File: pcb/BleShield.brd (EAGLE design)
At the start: 22.6 x 10 mm, 31 parts, among them U1 ARDUINO_SHIELDNOHOLES, Y1 32.768KHz, 10 PPM

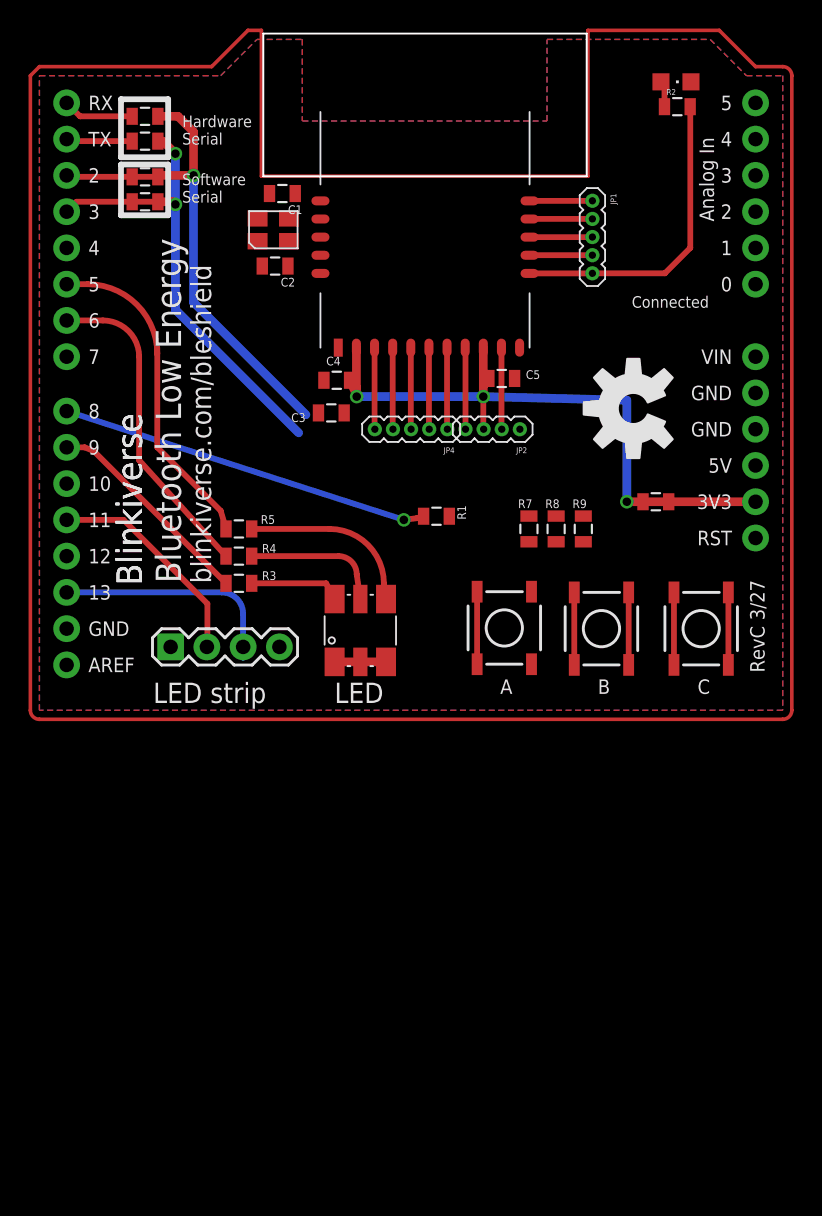
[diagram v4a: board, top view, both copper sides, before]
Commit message: Knocked out everything except crystal pad and RX/TX doublecheck.
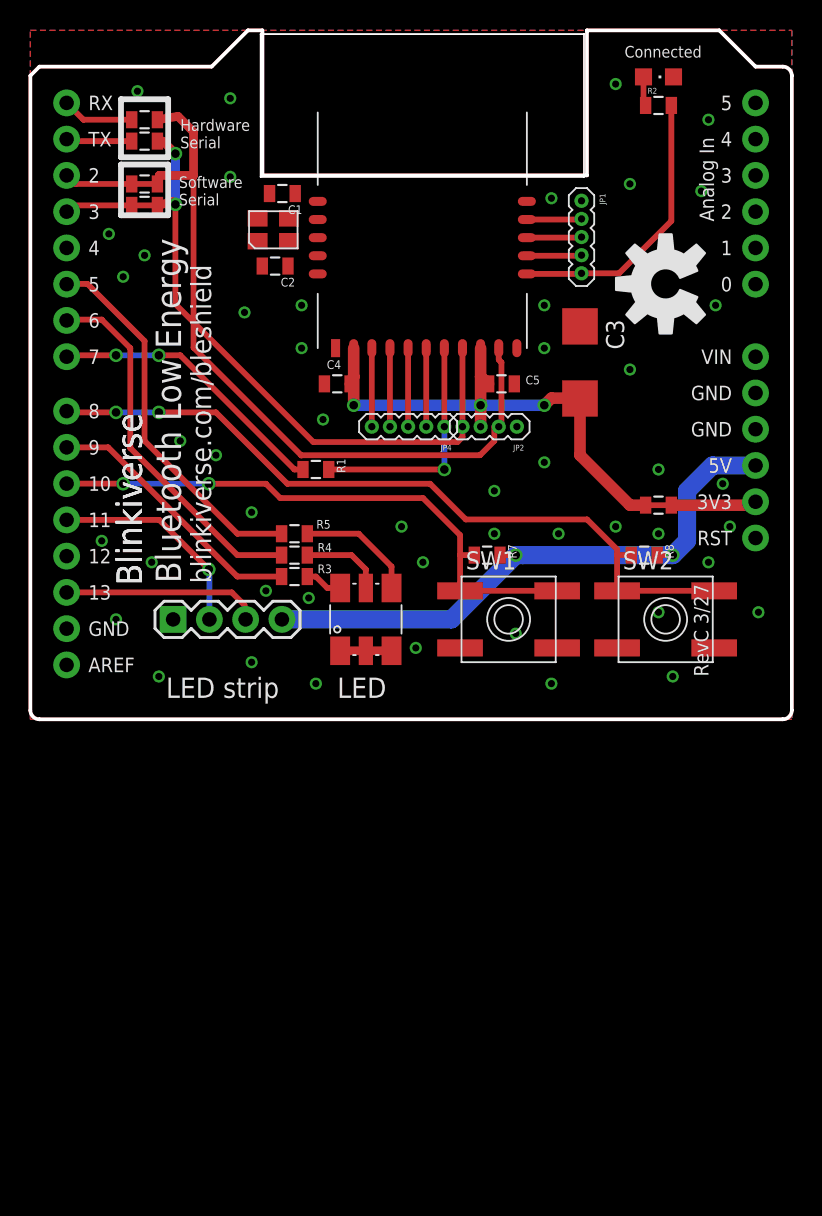
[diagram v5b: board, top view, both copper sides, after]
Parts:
- removed A, B, C: (no value), SparkFun:TACTILE_SWITCH_SMD
- removed R9: 10K, SparkFun:0805
- added SW1, SW2: SPST_TACT-EVQQ2, adafruit:EVQ-Q2
- C3: device SparkFun:0805 -> rcl:C/6032-28R
- moved C3 17.8 mm to (38.5, 25.0), turned to 270 degrees
- moved R1 9.06 mm to (20.0, 17.5)
- moved U$7 9.01 mm to (44.5, 30.5)
- moved R8 6.44 mm to (43.0, 11.5), turned to 0 degrees
- moved R3 3.92 mm to (18.5, 10.0)
- moved R5 3.91 mm to (18.5, 13.0)
- moved R4 3.90 mm to (18.5, 11.5)
- moved R7 3.45 mm to (32.0, 11.5), turned to 0 degrees
- moved LED_STRIP 1.94 mm to (10.0, 7.00)
- moved R2 1.32 mm to (44.0, 43.0)
- moved LED1 1.27 mm to (44.0, 45.0)
- moved RGB_LED 0.87 mm to (23.5, 7.00)
- moved JP1 0.76 mm to (38.6, 36.3)
- moved R12 0.50 mm to (8.00, 37.5)
- moved C5 0.38 mm to (33.0, 23.5)
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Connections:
- removed net SWITCH_C: C.3, C.4, R9.1, U1.D7
- net 3.3V: now also C3.+; no longer C3.2
- net 5V: no longer R9.2
- net GND: now also C3.-, SW1.A, SW1.A', SW2.A, SW2.A'; no longer A.1, A.2, B.1, B.2, C.1, C.2, C3.1
- net RESET: now also U1.D7; no longer U1.D8
- net SWITCH_A: now also SW1.B, SW1.B', U1.D10; no longer A.3, A.4, U1.D12
- net SWITCH_B: now also SW2.B, SW2.B', U1.D8; no longer B.3, B.4, U1.D4
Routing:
- net SWITCH_B: track 5.08 -> 53.3 mm, vias 0 -> 2
- net 5V: track 0.00 -> 41.9 mm, vias 0 -> 2
- net SWITCH_A: track 5.08 -> 40.9 mm, vias 0 -> 2
- net RX: track 40.7 -> 59.3 mm, vias 1 -> 0
- net GND: track 18.3 -> 3.92 mm, vias 0 -> 48
- net TX: track 38.4 -> 50.6 mm
- net N$1: track 5.74 -> 16.6 mm, vias 0 -> 1
- net RESET: track 26.2 -> 19.9 mm, vias 1 -> 2
- net SWITCH_C: track 5.08 -> 0.00 mm
- net N$2: track 6.47 -> 2.63 mm
- net N$6: track 9.64 -> 5.81 mm
- net LED_BLUE: track 15.1 -> 18.8 mm
- net N$5: track 12.0 -> 8.35 mm
- net LED_RED: track 22.4 -> 26.0 mm
- net LED_GREEN: track 23.0 -> 26.4 mm
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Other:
- board size 22.6 x 10 mm -> 53.3 x 48.3 mm

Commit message: Fix RX/TX line assignment
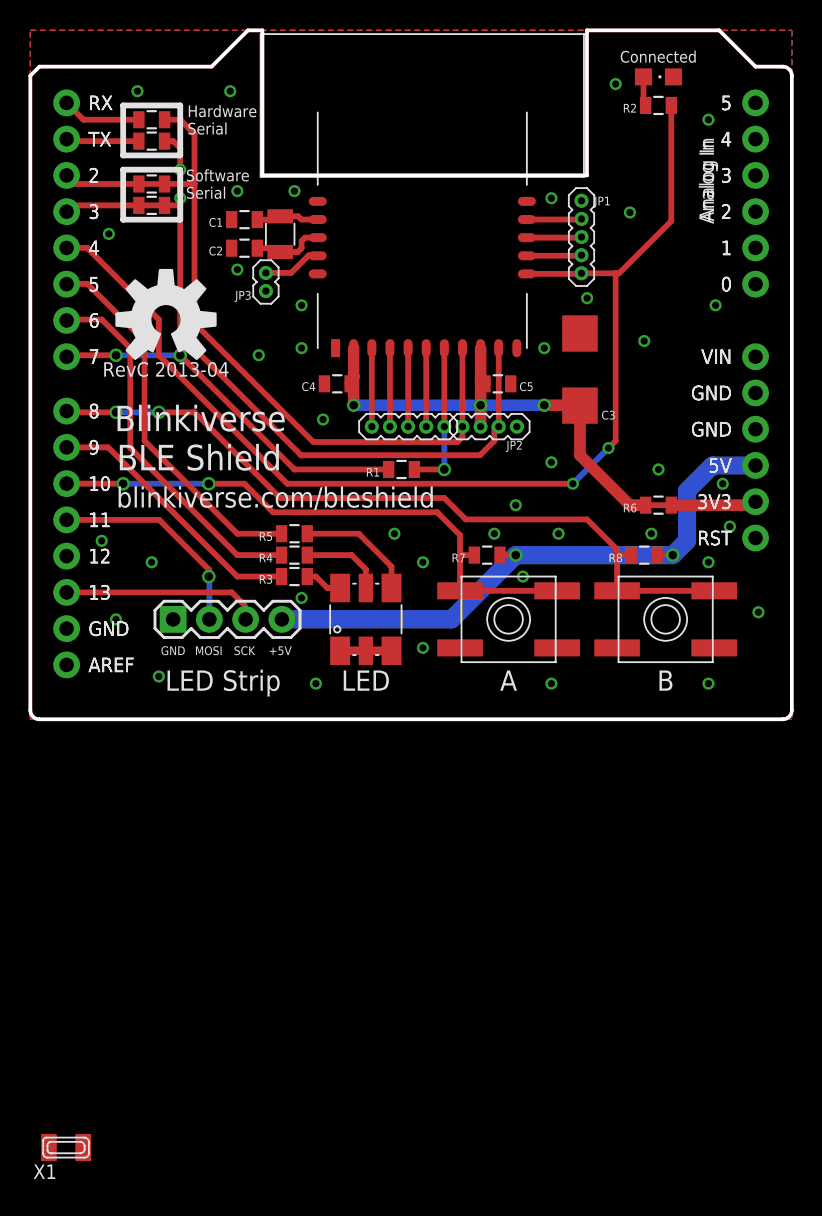
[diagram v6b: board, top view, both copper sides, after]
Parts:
- removed Y1: 32.768KHz, 10 PPM, blinkiverse:XS3225
- added JP3: (no value), BLE:1X02-1.27MM
- added Q1: 32.768K, 10ppm, blinkiverse:CRYSTAL_3215
- added X1: (no value), adafruit:XTAL3215
- moved U$7 35.1 mm to (9.50, 28.0), turned to 0 degrees
- moved R1 6.00 mm to (26.0, 17.5)
- moved C1 3.22 mm to (15.0, 35.0), turned to 0 degrees
- moved C2 2.48 mm to (15.0, 33.0), turned to 0 degrees
- moved C3 0.50 mm to (38.5, 24.5)
- moved R10 0.50 mm to (8.50, 42.0)
- moved R11 0.50 mm to (8.50, 40.5)
- moved R12 0.50 mm to (8.50, 37.5)
- moved R13 0.50 mm to (8.50, 36.0)
- moved C5 0.25 mm to (32.8, 23.5)
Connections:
- removed net N$9: JP1.5, R2.2, U$1.P0_7
- new net CONNECTED: JP1.5, R2.2, U$1.P0_7, U1.D4
- new net N$19: JP3.2, U$1.P2_0
- net GND: now also JP3.1
- net N$3: now also Q1.P$2; no longer Y1.P$3
- net N$4: now also Q1.P$1; no longer Y1.P$1
- net RX: now also JP2.4, U$1.P1_6/TX; no longer JP2.2, U$1.P1_7/RX
- net TX: now also JP2.2, U$1.P1_7/RX; no longer JP2.4, U$1.P1_6/TX
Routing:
- net CONNECTED: track 0.00 -> 79.5 mm, vias 0 -> 2
- net N$9: track 19.8 -> 0.00 mm
- net RESET: track 19.9 -> 25.9 mm
- net N$1: track 16.6 -> 10.6 mm
- net RX: track 59.3 -> 53.6 mm
- net N$4: track 0.00 -> 5.05 mm
- net TX: track 50.6 -> 55.2 mm
- net N$3: track 0.00 -> 4.42 mm
- net N$19: track 0.00 -> 4.15 mm
- net MOSI: track 14.9 -> 15.8 mm
- net 3.3V: track 44.7 -> 43.8 mm
- net N$11: track 4.62 -> 5.12 mm
- net N$10: track 5.05 -> 5.55 mm
- net GND: vias 48 -> 41
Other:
- board text added: "+5V"
- board text added: "0"
- board text added: "1"
- board text added: "10"
- board text added: "11"
- board text added: "12"
- board text added: "13"
- board text added: "2"
- board text added: "3"
- board text added: "3V3"
- board text added: "4"
- board text added: "5"
- board text added: "5V"
- board text added: "6"
- board text added: "7"
- board text added: "8"
- board text added: "9"
- board text added: "A"
- board text added: "AREF"
- board text added: "Analog In"
- board text added: "B"
- board text added: "BLE Shield"
- board text added: "GND"
- board text added: "LED Strip"
- board text added: "MOSI"
- board text added: "RST"
- board text added: "RX"
- board text added: "RevC 2013-04"
- board text added: "SCK"
- board text added: "TX"
- board text added: "VIN"
- board text removed: "Bluetooth Low Energy"
- board text removed: "LED strip"
- board text removed: "RevC 3/27"

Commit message: RevC release candidate
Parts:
- removed X1: (no value), adafruit:XTAL3215
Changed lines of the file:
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@@
 <layer number="14" name="Route14" color="1" fill="6" visible="no" active="no"/>
 <layer number="15" name="Route15" color="4" fill="6" visible="no" active="no"/>
-<layer number="16" name="Bottom" color="1" fill="1" visible="yes" active="yes"/>
+<layer number="16" name="Bottom" color="1" fill="1" visible="no" active="yes"/>
 <layer number="17" name="Pads" color="2" fill="1" visible="yes" active="yes"/>
 <layer number="18" name="Vias" color="2" fill="1" visible="yes" active="yes"/>
-<layer number="19" name="Unrouted" color="6" fill="1" visible="yes" active="yes"/>
-<layer number="20" name="Dimension" color="15" fill="1" visible="no" active="yes"/>
+<layer number="19" name="Unrouted" color="6" fill="1" visible="no" active="yes"/>
+<layer number="20" name="Dimension" color="15" fill="1" visible="yes" active="yes"/>
 <layer number="21" name="tPlace" color="7" fill="1" visible="no" active="yes"/>
 <layer number="22" name="bPlace" color="7" fill="1" visible="no" active="yes"/>
-<layer number="23" name="tOrigins" color="15" fill="1" visible="yes" active="yes"/>
+<layer number="23" name="tOrigins" color="15" fill="1" visible="no" active="yes"/>
 <layer number="24" name="bOrigins" color="15" fill="1" visible="no" active="yes"/>
 <layer number="25" name="tNames" color="7" fill="1" visible="yes" active="yes"/>
@@
 <layer number="27" name="tValues" color="7" fill="1" visible="no" active="yes"/>
 <layer number="28" name="bValues" color="7" fill="1" visible="no" active="yes"/>
-<layer number="29" name="tStop" color="7" fill="3" visible="yes" active="yes"/>
+<layer number="29" name="tStop" color="7" fill="3" visible="no" active="yes"/>
 <layer number="30" name="bStop" color="7" fill="6" visible="no" active="yes"/>
-<layer number="31" name="tCream" color="7" fill="4" visible="yes" active="yes"/>
+<layer number="31" name="tCream" color="7" fill="4" visible="no" active="yes"/>
 <layer number="32" name="bCream" color="7" fill="5" visible="no" active="yes"/>
 <layer number="33" name="tFinish" color="6" fill="3" visible="no" active="yes"/>
@@
 <layer number="109" name="fp9" color="7" fill="1" visible="no" active="yes"/>
 <layer number="110" name="fp0" color="7" fill="1" visible="no" active="yes"/>
-<layer number="111" name="LPC17xx" color="7" fill="1" visible="yes" active="yes"/>
-<layer number="112" name="tSilk" color="7" fill="1" visible="yes" active="yes"/>
+<layer number="111" name="LPC17xx" color="7" fill="1" visible="no" active="yes"/>
+<layer number="112" name="tSilk" color="7" fill="1" visible="no" active="yes"/>
 <layer number="116" name="Patch_BOT" color="9" fill="4" visible="no" active="yes"/>
 <layer number="121" name="_tsilk" color="7" fill="1" visible="no" active="yes"/>
@@
 <layer number="124" name="bTestmark" color="7" fill="1" visible="no" active="yes"/>
 <layer number="125" name="_tNames" color="7" fill="1" visible="no" active="yes"/>
-<layer number="126" name="_bNames" color="7" fill="1" visible="yes" active="yes"/>
-<layer number="127" name="_tValues" color="7" fill="1" visible="yes" active="yes"/>
-<layer number="128" name="_bValues" color="7" fill="1" visible="yes" active="yes"/>
+<layer number="126" name="_bNames" color="7" fill="1" visible="no" active="yes"/>
+<layer number="127" name="_tValues" color="7" fill="1" visible="no" active="yes"/>
+<layer number="128" name="_bValues" color="7" fill="1" visible="no" active="yes"/>
 <layer number="131" name="tAdjust" color="7" fill="1" visible="no" active="yes"/>
 <layer number="132" name="bAdjust" color="7" fill="1" visible="no" active="yes"/>
 <layer number="144" name="Drill_legend" color="7" fill="1" visible="no" active="yes"/>
 <layer number="151" name="HeatSink" color="7" fill="1" visible="no" active="yes"/>
-<layer number="152" name="_bDocu" color="7" fill="1" visible="yes" active="yes"/>
+<layer number="152" name="_bDocu" color="7" fill="1" visible="no" active="yes"/>
 <layer number="199" name="Contour" color="7" fill="1" visible="no" active="yes"/>
 <layer number="200" name="200bmp" color="1" fill="10" visible="no" active="yes"/>
@@
 <layer number="223" name="223bmp" color="24" fill="1" visible="no" active="no"/>
 <layer number="224" name="224bmp" color="25" fill="1" visible="no" active="no"/>
-<layer number="248" name="Housing" color="7" fill="1" visible="yes" active="yes"/>
-<layer number="249" name="Edge" color="7" fill="1" visible="yes" active="yes"/>
+<layer number="248" name="Housing" color="7" fill="1" visible="no" active="yes"/>
+<layer number="249" name="Edge" color="7" fill="1" visible="no" active="yes"/>
 <layer number="250" name="Descript" color="3" fill="1" visible="no" active="no"/>
 <layer number="251" name="SMDround" color="12" fill="11" visible="no" active="no"/>
@@
 </element>
 <element name="Q1" library="blinkiverse" package="CRYSTAL_3215" value="32.768K, 10ppm" x="17.5" y="34" rot="R90"/>
-<element name="X1" library="adafruit" package="XTAL3215" value="" x="2.5" y="-30"/>
 </elements>
 <signals>

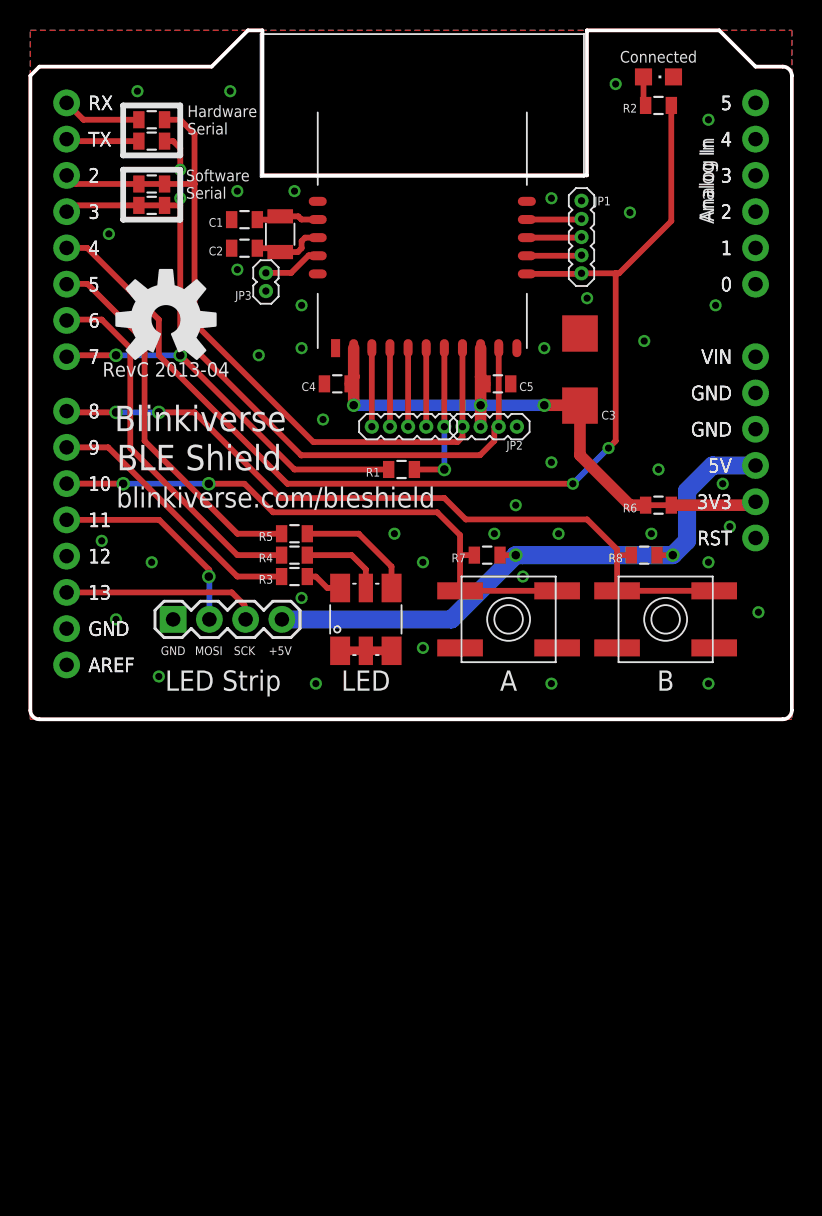
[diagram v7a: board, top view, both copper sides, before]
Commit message: On Samson's recommendation, add ground planes on top&bottom layers under module.
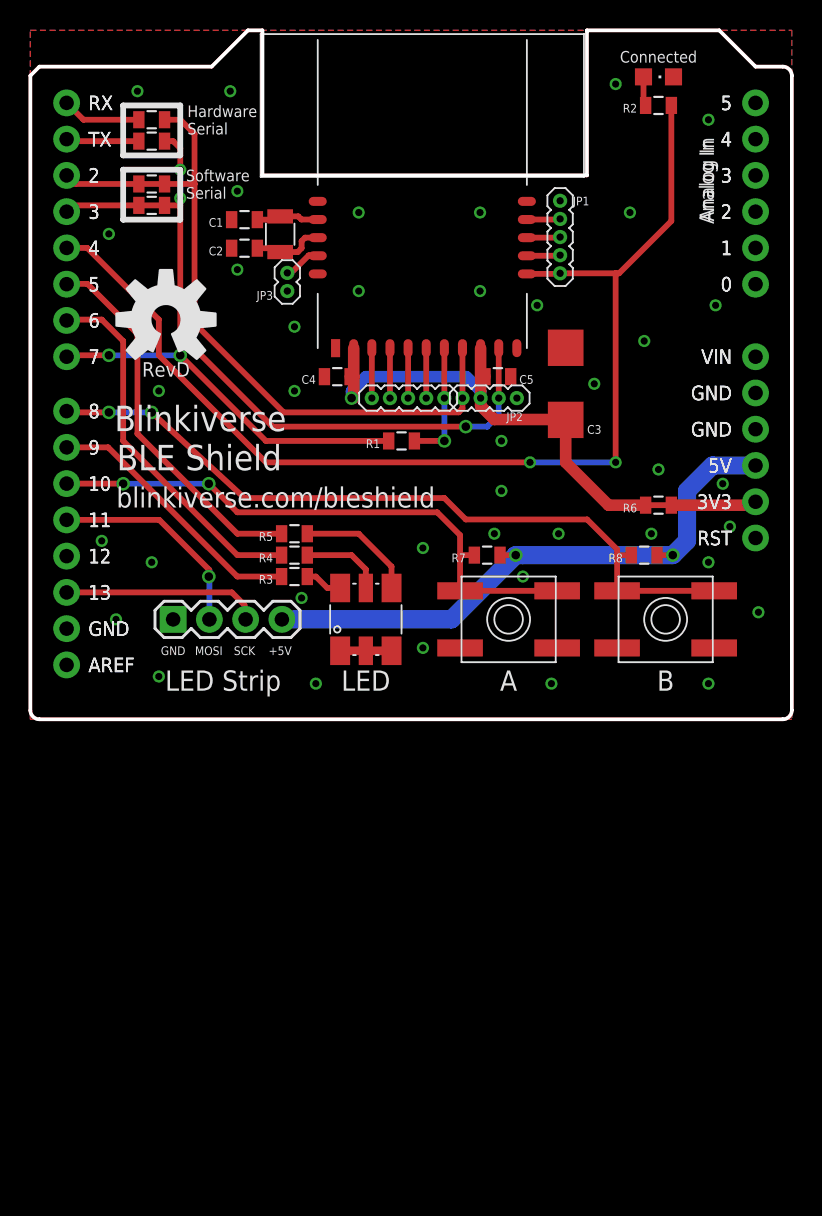
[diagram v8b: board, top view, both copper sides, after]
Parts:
- moved JP2 2.00 mm to (34.1, 22.5)
- moved JP4 2.00 mm to (29.0, 22.5)
- moved R1 2.00 mm to (26.0, 19.5)
- moved JP1 1.50 mm to (37.1, 36.3)
- moved JP3 1.50 mm to (18.0, 30.0)
- moved C3 1.41 mm to (37.5, 23.5)
- moved C4 0.50 mm to (21.5, 24.0)
- moved C5 0.50 mm to (32.8, 24.0)
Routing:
- net RX: track 53.6 -> 50.7 mm
- net TX: track 55.2 -> 52.5 mm, vias 2 -> 3
- net N$8: track 5.50 -> 3.50 mm
- net N$14: track 5.50 -> 3.50 mm
- net N$13: track 5.50 -> 3.50 mm
- net N$12: track 5.50 -> 3.50 mm
- net N$1: track 10.6 -> 8.60 mm
- net N$18: track 3.85 -> 2.35 mm
- net N$16: track 3.85 -> 2.35 mm
- net N$15: track 3.85 -> 2.35 mm
- net N$19: track 4.15 -> 2.65 mm
- net RESET: track 25.9 -> 25.1 mm
- net 3.3V: track 43.8 -> 43.2 mm, vias 3 -> 1
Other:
- board text added: "RevD"
- board text removed: "RevC 2013-04"
